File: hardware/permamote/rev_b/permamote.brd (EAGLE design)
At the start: 27 x 60 mm, 125 parts, among them J1 TC2030-JLINK-NL, J5 MICRO_USB_B_HIROSE_ZX62R-B-5P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, Q1 PMDXB950UPEL, Q10 PMDXB950UPEL, Q2 PMDXB950UPEL, Q3 PMDXB950UPEL, Q4 PMDXB950UPEL, Q5 PMDXB950UPEL, Q6 PMDXB950UPEL, Q7 PMDXB950UPEL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

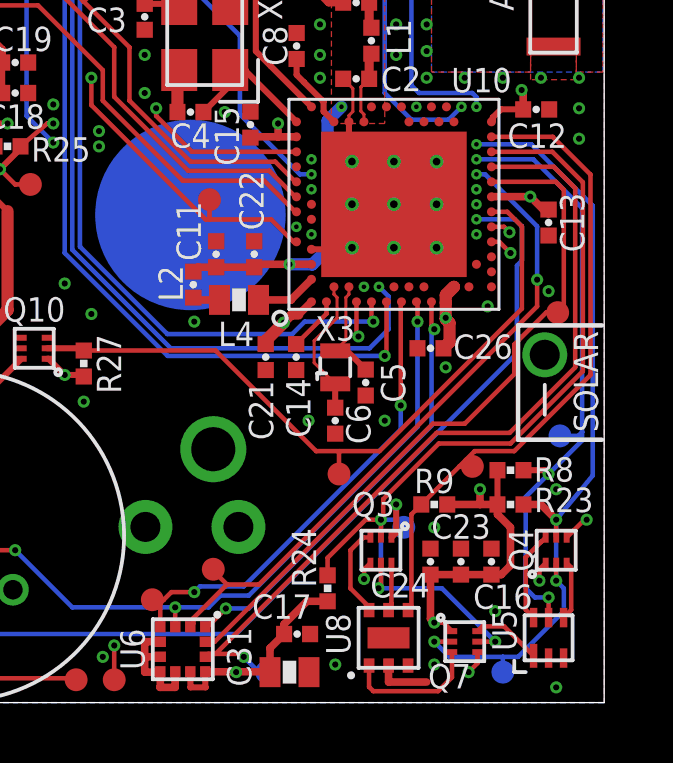
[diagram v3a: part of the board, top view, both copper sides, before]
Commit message: Switch to TCS34725 color sensor
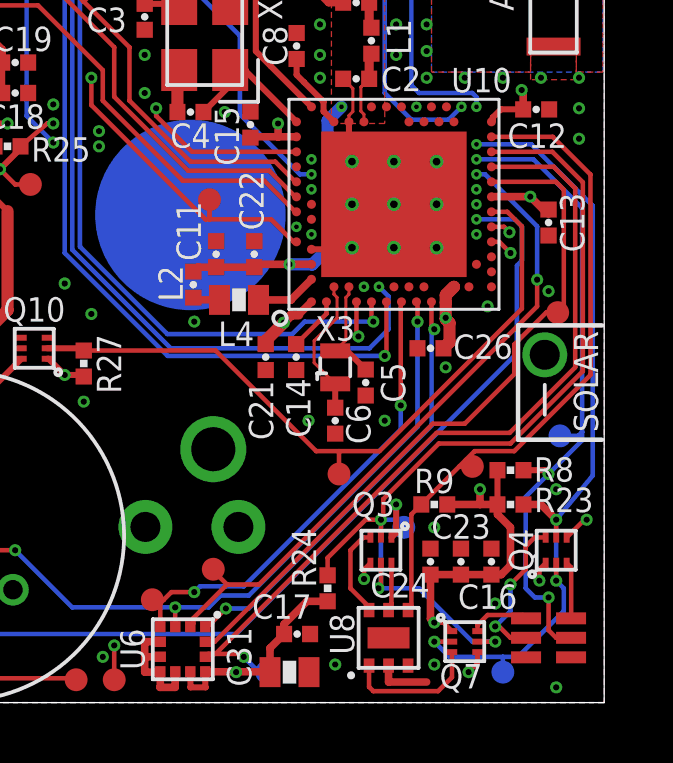
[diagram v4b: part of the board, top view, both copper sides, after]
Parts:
- removed U5: ISL29125, chips:ODFN-6-1.5MMX1.6MM
- added U12: TCS34725, chips:FN-6
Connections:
- net !CLR_INT: now also U12.5; no longer U5.5
- net GND: now also U12.3; no longer U5.3
- net N$31: now also U12.1; no longer U5.1
- net N$54: now also U12.6; no longer U5.4
- net N$55: now also U12.2; no longer U5.6
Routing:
- net N$55: track 3.06 -> 5.06 mm, vias 0 -> 2
- net !CLR_INT: track 20.9 -> 22.2 mm
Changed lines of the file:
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@@
 <?xml version="1.0" encoding="utf-8"?>
 <!DOCTYPE eagle SYSTEM "eagle.dtd">
-<eagle version="9.0.0">
+<eagle version="9.0.1">
 <drawing>
 <settings>
@@
 <attribute name="NAME" x="23.114" y="5.842" size="0.8128" layer="26" font="vector" ratio="12" rot="MR90"/>
 </element>
-<element name="U5" library="chips" package="ODFN-6-1.5MMX1.6MM" value="ISL29125" x="25.146" y="2.159" smashed="yes" rot="R90">
-<attribute name="DIGIKEY" value="ISL29125IROZ-T7ACT-ND " x="25.146" y="2.159" size="1.778" layer="27" rot="R90" display="off"/>
-<attribute name="MANUFACTURER" value="INTERSIL" x="25.146" y="2.159" size="1.778" layer="27" rot="R90" display="off"/>
-<attribute name="MPN" value="ISL29125IROZ-T7A" x="25.146" y="2.159" size="1.778" layer="27" rot="R90" display="off"/>
-<attribute name="NAME" x="23.268" y="2.409" size="0.8128" layer="25" font="vector" ratio="12" rot="R90" align="top-center"/>
-</element>
 <element name="U8" library="chips" package="UDFN-6-EXPOSED" value="MAX44009" x="19.812" y="2.159" smashed="yes" rot="R90">
 <attribute name="DIGIKEY" value="MAX44009EDT+TCT-ND" x="19.812" y="2.159" size="1.778" layer="27" rot="R90" display="off"/>
 <attribute name="MANUFACTURER" value="MAXIM" x="19.812" y="2.159" size="1.778" layer="27" rot="R90" display="off"/>
 <attribute name="MPN" value="MAX44009EDT+T" x="19.812" y="2.159" size="1.778" layer="27" rot="R90" display="off"/>
-<attribute name="NAME" x="18.542" y="2.286" size="0.8128" layer="25" font="vector" ratio="12" rot="R90" align="bottom-center"/>
+<attribute name="NAME" x="18.669" y="2.286" size="0.8128" layer="25" font="vector" ratio="12" rot="R90" align="bottom-center"/>
 </element>
 <element name="C23" library="passives" package="0402_CAP" value="1uF" x="22.225" y="4.699" smashed="yes" rot="R90">
@@
 <attribute name="DIGIKEY" value="490-6328-1-ND" x="23.241" y="4.699" size="1.778" layer="27" rot="R90" display="off"/>
 <attribute name="MPN" value="GRM155R71C104KA88J " x="23.241" y="4.699" size="1.778" layer="27" rot="R90" display="off"/>
-<attribute name="NAME" x="23.622" y="3.937" size="0.8128" layer="25" font="vector" ratio="12" rot="R180" align="bottom-center"/>
+<attribute name="NAME" x="23.114" y="3.937" size="0.8128" layer="25" font="vector" ratio="12" rot="R180" align="bottom-center"/>
 </element>
 <element name="C24" library="passives" package="0402_CAP" value="1uF" x="21.209" y="4.699" smashed="yes" rot="R90">
@@
 <attribute name="MANUFACTURER" value="NEXPERIA" x="22.352" y="2.032" size="1.778" layer="27" display="off"/>
 <attribute name="MPN" value="PMDXB950UPELZ" x="22.352" y="2.032" size="1.778" layer="27" display="off"/>
-<attribute name="NAME" x="21.844" y="1.286" size="0.8128" layer="25" font="vector" ratio="12" rot="R180" align="bottom-center"/>
+<attribute name="NAME" x="22.225" y="1.286" size="0.8128" layer="25" font="vector" ratio="12" rot="R180" align="bottom-center"/>
 <attribute name="VALUE" x="22.352" y="1.032" size="1.016" layer="27" font="vector" ratio="12" align="top-center"/>
 </element>
@@
 <element name="TP26" library="headers" package="PAD.03X.03" value="TEST-POINT" x="26.035" y="39.116" rot="MR0"/>
 <element name="TP27" library="headers" package="PAD.03X.03" value="TEST-POINT" x="26.035" y="37.084" rot="MR0"/>
+<element name="U12" library="chips" package="FN-6" value="TCS34725" x="25.146" y="2.159" smashed="yes">
+<attribute name="DIGIKEY" value="TCS34725FNCT-ND" x="25.146" y="2.159" size="1.778" layer="27" display="off"/>
+<attribute name="NAME" x="26.654" y="4.315" size="0.8128" layer="23" font="vector" ratio="12" rot="R180"/>
+</element>
 </elements>
 <signals>
@@
 <contactref element="U7" pad="3"/>
 <contactref element="C30" pad="2"/>
-<contactref element="U5" pad="3"/>
 <contactref element="U8" pad="2"/>
 <contactref element="U8" pad="EP"/>
@@
 <via x="18.034" y="1.27" extent="1-16" drill="0.2032"/>
 <via x="25.4" y="7.112" extent="1-16" drill="0.2032"/>
-<via x="23.368" y="3.048" extent="1-16" drill="0.2032"/>
+<via x="23.368" y="3.302" extent="1-16" drill="0.2032"/>
 <via x="25.4" y="0.508" extent="1-16" drill="0.2032"/>
 <via x="20.066" y="23.622" extent="1-16" drill="0.2032"/>
@@
 <wire x1="19.812" y1="1.234" x2="19.812" y2="0.6858" width="0.254" layer="1"/>
 <wire x1="19.812" y1="0.6858" x2="21.082" y2="0.6858" width="0.254" layer="1"/>
+<contactref element="U12" pad="3"/>
 </signal>
 <signal name="N$8">
@@
 </signal>
 <signal name="!CLR_INT">
-<contactref element="U5" pad="5"/>
 <contactref element="R8" pad="1"/>
 <contactref element="U10" pad="AC19"/>
 <via x="22.742" y="18.11" extent="1-16" drill="0.1524"/>
 <via x="25.146" y="3.5052" extent="1-16" drill="0.2032"/>
-<wire x1="25.146" y1="2.834" x2="25.146" y2="3.5052" width="0.1524" layer="1"/>
 <wire x1="25.146" y1="3.5052" x2="24.6888" y2="3.5052" width="0.1524" layer="16"/>
 <wire x1="24.6888" y1="3.5052" x2="24.384" y2="3.81" width="0.1524" layer="16"/>
@@
 <wire x1="25.527" y1="8.89" x2="26.136971875" y2="8.89" width="0.1524" layer="16"/>
 <wire x1="26.136971875" y1="8.89" x2="26.263971875" y2="9.017" width="0.1524" layer="16"/>
+<contactref element="U12" pad="5"/>
+<wire x1="25.896" y1="2.159" x2="25.4" y2="2.159" width="0.1524" layer="1"/>
+<wire x1="25.4" y1="2.159" x2="25.146" y2="2.413" width="0.1524" layer="1"/>
+<wire x1="25.146" y1="2.413" x2="25.146" y2="3.5052" width="0.1524" layer="1"/>
 </signal>
 <signal name="!LT_INT">
@@
 <via x="23.368" y="2.032" extent="1-16" drill="0.2032"/>
 <wire x1="19.4762" y1="3.81" x2="19.558" y2="3.81" width="0.1524" layer="16"/>
-<wire x1="19.558" y1="3.81" x2="21.59" y2="3.81" width="0.1524" layer="16"/>
-<wire x1="21.59" y1="3.81" x2="23.368" y2="2.032" width="0.1524" layer="16"/>
 <wire x1="19.558" y1="5.505" x2="19.558" y2="6.096" width="0.1524" layer="1"/>
 <via x="19.558" y="6.096" extent="1-16" drill="0.2032"/>
@@
 <wire x1="26.289" y1="11.049" x2="23.876" y2="8.636" width="0.1524" layer="1"/>
 <wire x1="23.876" y1="8.636" x2="21.4873375" y2="8.636" width="0.1524" layer="1"/>
-<wire x1="26.289" y1="17.344" x2="26.289" y2="16.383" width="0.1524" layer="1"/>
-<wire x1="26.289" y1="16.383" x2="26.289" y2="11.049" width="0.1524" layer="1"/>
+<wire x1="26.289" y1="17.344" x2="26.289" y2="11.049" width="0.1524" layer="1"/>
+<wire x1="23.368" y1="2.032" x2="22.606" y2="2.032" width="0.1524" layer="16"/>
+<wire x1="20.828" y1="3.81" x2="19.558" y2="3.81" width="0.1524" layer="16"/>
+<wire x1="22.606" y1="2.032" x2="20.828" y2="3.81" width="0.1524" layer="16"/>
 </signal>
 <signal name="VREF_SAMP">
@@
 </signal>
 <signal name="N$31">
-<contactref element="U5" pad="1"/>
 <contactref element="Q7" pad="6"/>
-<wire x1="22.777" y1="2.382" x2="22.935" y2="2.54" width="0.1524" layer="1"/>
-<wire x1="23.665" y1="2.54" x2="24.646" y2="1.559" width="0.1524" layer="1"/>
-<wire x1="22.935" y1="2.54" x2="23.665" y2="2.54" width="0.1524" layer="1"/>
+<contactref element="U12" pad="1"/>
+<wire x1="22.777" y1="2.382" x2="22.777" y2="2.584" width="0.1524" layer="1"/>
+<wire x1="22.777" y1="2.584" x2="23.114" y2="2.921" width="0.1524" layer="1"/>
+<wire x1="23.114" y1="2.921" x2="24.284" y2="2.921" width="0.1524" layer="1"/>
+<wire x1="24.284" y1="2.921" x2="24.396" y2="2.809" width="0.1524" layer="1"/>
 </signal>
 <signal name="N$20">
@@
 <signal name="N$54">
 <contactref element="Q4" pad="3"/>
-<contactref element="U5" pad="4"/>
-<wire x1="25.9" y1="4.505" x2="25.75" y2="4.655" width="0.1524" layer="1"/>
-<wire x1="25.646" y1="2.834" x2="25.9" y2="3.088" width="0.1524" layer="1"/>
-<wire x1="25.9" y1="3.088" x2="25.9" y2="4.505" width="0.1524" layer="1"/>
+<wire x1="25.75" y1="4.655" x2="25.9" y2="4.505" width="0.1524" layer="1"/>
+<contactref element="U12" pad="6"/>
+<wire x1="25.9" y1="2.813" x2="25.896" y2="2.809" width="0.1524" layer="1"/>
+<wire x1="25.9" y1="4.505" x2="25.9" y2="2.813" width="0.1524" layer="1"/>
 </signal>
 <signal name="N$55">
 <contactref element="Q4" pad="6"/>
-<contactref element="U5" pad="6"/>
-<wire x1="25.05" y1="5.505" x2="24.902" y2="5.357" width="0.1524" layer="1"/>
-<wire x1="24.902" y1="5.357" x2="24.89739375" y2="5.357" width="0.1524" layer="1"/>
-<wire x1="24.384" y1="4.84360625" x2="24.89739375" y2="5.357" width="0.1524" layer="1"/>
-<wire x1="24.646" y1="2.834" x2="24.384" y2="3.096" width="0.1524" layer="1"/>
-<wire x1="24.384" y1="3.096" x2="24.384" y2="4.84360625" width="0.1524" layer="1"/>
+<contactref element="U12" pad="2"/>
+<via x="23.368" y="2.54" extent="1-16" drill="0.2032"/>
+<wire x1="23.368" y1="2.54" x2="23.495" y2="2.54" width="0.1524" layer="1"/>
+<wire x1="23.495" y1="2.54" x2="23.876" y2="2.159" width="0.1524" layer="1"/>
+<wire x1="23.876" y1="2.159" x2="24.396" y2="2.159" width="0.1524" layer="1"/>
+<via x="23.876" y="3.937" extent="1-16" drill="0.2032"/>
+<wire x1="23.876" y1="3.937" x2="23.876" y2="3.048" width="0.1524" layer="16"/>
+<wire x1="23.876" y1="3.048" x2="23.368" y2="2.54" width="0.1524" layer="16"/>
+<wire x1="25.05" y1="5.505" x2="24.682" y2="5.505" width="0.1524" layer="1"/>
+<wire x1="24.682" y1="5.505" x2="24.384" y2="5.207" width="0.1524" layer="1"/>
+<wire x1="24.384" y1="5.207" x2="24.384" y2="4.445" width="0.1524" layer="1"/>
+<wire x1="24.384" y1="4.445" x2="23.876" y2="3.937" width="0.1524" layer="1"/>
 </signal>
 <signal name="LBST">

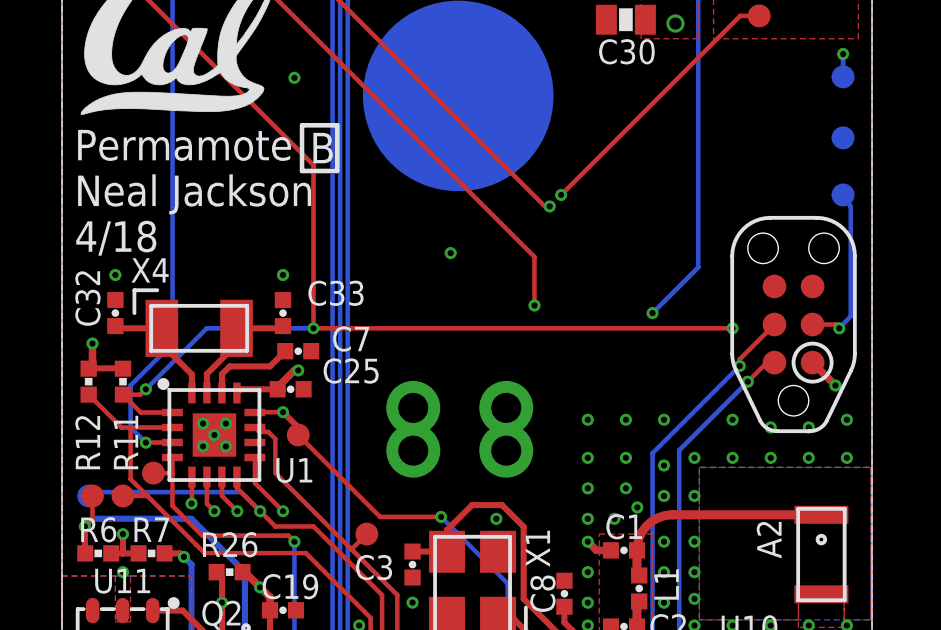
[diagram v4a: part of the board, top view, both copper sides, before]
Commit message: move programmer
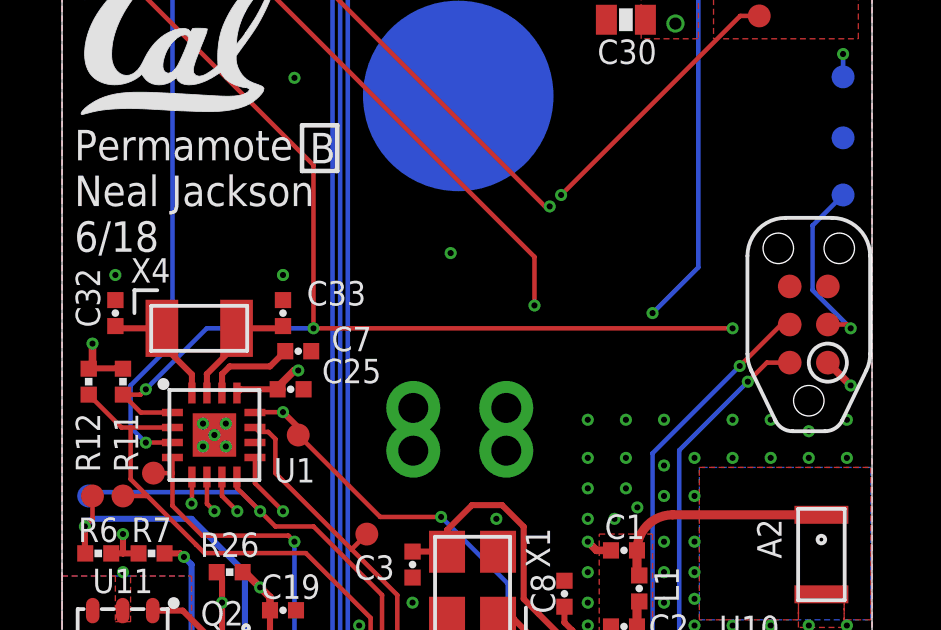
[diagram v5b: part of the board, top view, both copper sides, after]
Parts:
- moved J1 0.51 mm to (24.9, 30.9)
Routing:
- net !RST: track 65.3 -> 66.3 mm
- net SWDIO: track 13.1 -> 13.6 mm
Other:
- board text added: "Permamote Neal Jackson 6/18"
- board text removed: "Permamote Neal Jackson 4/18"
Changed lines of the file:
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@@
 <text x="0.413" y="37.349" size="1.016" layer="25" font="vector" ratio="12" align="top-left">Permamote
 Neal Jackson
-4/18</text>
+6/18</text>
 <polygon width="0.1016" layer="41">
 <vertex x="12.446" y="1.7907"/>
@@
 <attribute name="NAME" x="7.62" y="21.717" size="0.8128" layer="25" font="vector" ratio="12" align="bottom-center"/>
 </element>
-<element name="J1" library="connector" package="TC2030-IDC-NL" value="TC2030-JLINK-NL" x="24.384" y="30.861" smashed="yes" rot="R90">
-<attribute name="VALUE" x="30.4165" y="30.861" size="1.016" layer="27" font="vector" ratio="12" rot="R90" align="bottom-center"/>
+<element name="J1" library="connector" package="TC2030-IDC-NL" value="TC2030-JLINK-NL" x="24.892" y="30.861" smashed="yes" rot="R90">
+<attribute name="VALUE" x="30.9245" y="30.861" size="1.016" layer="27" font="vector" ratio="12" rot="R90" align="bottom-center"/>
 </element>
 <element name="R23" library="passives" package="0402_RES" value="100M" x="23.876" y="6.604" smashed="yes" rot="R180">
@@
 <via x="20.066" y="27.686" extent="1-16" drill="0.2032"/>
 <via x="22.352" y="27.686" extent="1-16" drill="0.2032"/>
-<via x="23.622" y="27.432" extent="1-16" drill="0.2032"/>
-<via x="24.892" y="27.432" extent="1-16" drill="0.2032"/>
+<via x="23.622" y="27.686" extent="1-16" drill="0.2032"/>
+<via x="24.892" y="27.305" extent="1-16" drill="0.2032"/>
 <via x="26.162" y="27.686" extent="1-16" drill="0.2032"/>
 <contactref element="U2" pad="5"/>
@@
 <wire x1="6.93293125" y1="21.336" x2="6.93293125" y2="21.76906875" width="0.254" layer="1"/>
 <wire x1="6.93293125" y1="21.76906875" x2="6.604" y2="22.098" width="0.254" layer="1"/>
-<via x="25.781" y="28.829" extent="1-16" drill="0.2032"/>
+<via x="26.289" y="28.829" extent="1-16" drill="0.2032"/>
 <wire x1="16.129" y1="19.304" x2="16.129" y2="18.86" width="0.254" layer="1"/>
 <wire x1="16.33093125" y1="2.286" x2="16.33093125" y2="2.61493125" width="0.254" layer="1"/>
@@
 <wire x1="9.017" y1="10.922" x2="9.59993125" y2="10.922" width="0.2032" layer="1"/>
 <wire x1="9.59993125" y1="10.922" x2="9.652" y2="10.86993125" width="0.2032" layer="1"/>
-<wire x1="25.019" y1="29.591" x2="25.781" y2="28.829" width="0.254" layer="1"/>
+<wire x1="25.527" y1="29.591" x2="26.289" y2="28.829" width="0.254" layer="1"/>
 <wire x1="21.992" y1="13.86" x2="21.717" y2="13.585" width="0.4064" layer="1"/>
 <wire x1="21.717" y1="13.585" x2="21.717" y2="13.335" width="0.4064" layer="1"/>
@@
 <via x="22.742" y="16.61" extent="1-16" drill="0.1524"/>
 <contactref element="SJ3" pad="1"/>
-<wire x1="22.352" y1="30.734" x2="25.908" y2="30.734" width="0.1524" layer="15"/>
-<via x="25.908" y="30.734" extent="1-16" drill="0.2032"/>
-<wire x1="25.908" y1="30.734" x2="25.781" y2="30.861" width="0.1524" layer="1"/>
-<wire x1="25.781" y1="30.861" x2="25.019" y2="30.861" width="0.1524" layer="1"/>
+<wire x1="22.352" y1="30.734" x2="26.289" y2="30.734" width="0.1524" layer="15"/>
+<via x="26.289" y="30.734" extent="1-16" drill="0.2032"/>
+<wire x1="26.289" y1="30.734" x2="26.162" y2="30.861" width="0.1524" layer="1"/>
+<wire x1="26.162" y1="30.861" x2="25.527" y2="30.861" width="0.1524" layer="1"/>
 <wire x1="2.032" y1="28.52293125" x2="2.62693125" y2="27.928" width="0.1524" layer="1"/>
 <wire x1="2.62693125" y1="27.928" x2="3.68" y2="27.928" width="0.1524" layer="1"/>
@@
 <wire x1="20.574" y1="28.956" x2="22.352" y2="30.734" width="0.1524" layer="15"/>
 <wire x1="20.574" y1="20.574" x2="20.574" y2="28.956" width="0.1524" layer="15"/>
-<wire x1="25.908" y1="30.734" x2="25.908" y2="30.7467625" width="0.1524" layer="16"/>
-<wire x1="25.908" y1="30.7467625" x2="26.289" y2="31.1277625" width="0.1524" layer="16"/>
-<wire x1="26.289" y1="31.1277625" x2="26.289" y2="34.798" width="0.1524" layer="16"/>
 <wire x1="2.794" y1="28.702" x2="4.826" y2="30.734" width="0.1524" layer="16"/>
-<wire x1="26.289" y1="34.798" x2="26.035" y2="35.179" width="0.1524" layer="16"/>
 <wire x1="4.826" y1="30.734" x2="8.382" y2="30.734" width="0.1524" layer="16"/>
 <via x="8.382" y="30.734" extent="1-16" drill="0.2032"/>
@@
 <wire x1="1.27" y1="43.2871" x2="8.382" y2="36.1751" width="0.1524" layer="1"/>
 <wire x1="8.382" y1="36.1751" x2="8.382" y2="30.734" width="0.1524" layer="1"/>
+<wire x1="26.035" y1="35.179" x2="25.019" y2="34.163" width="0.1524" layer="16"/>
+<wire x1="25.019" y1="34.163" x2="25.019" y2="32.004" width="0.1524" layer="16"/>
+<wire x1="25.019" y1="32.004" x2="26.289" y2="30.734" width="0.1524" layer="16"/>
 </signal>
 <signal name="!RTC_IRQ1">
@@
 <wire x1="20.828" y1="20.32" x2="22.606" y2="20.32" width="0.1524" layer="16"/>
 <wire x1="22.86" y1="28.956" x2="20.574" y2="26.67" width="0.1524" layer="16"/>
-<wire x1="22.86" y1="28.956" x2="23.495" y2="29.591" width="0.1524" layer="1"/>
-<wire x1="23.495" y1="29.591" x2="23.749" y2="29.591" width="0.1524" layer="1"/>
 <via x="22.86" y="28.956" extent="1-16" drill="0.2032"/>
 <wire x1="20.574" y1="26.67" x2="20.574" y2="20.574" width="0.1524" layer="16"/>
 <wire x1="20.574" y1="20.574" x2="20.828" y2="20.32" width="0.1524" layer="16"/>
+<wire x1="22.86" y1="28.956" x2="23.495" y2="29.591" width="0.1524" layer="1"/>
+<wire x1="23.495" y1="29.591" x2="24.257" y2="29.591" width="0.1524" layer="1"/>
 </signal>
 <signal name="RTC_CS">
@@
 <contactref element="U10" pad="AA24"/>
 <via x="22.591865625" y="29.478134375" extent="1-16" drill="0.2032"/>
-<wire x1="23.749" y1="30.861" x2="22.591865625" y2="29.703865625" width="0.1524" layer="1"/>
-<wire x1="22.591865625" y1="29.703865625" x2="22.591865625" y2="29.478134375" width="0.1524" layer="1"/>
 <via x="22.242" y="19.86" extent="1-16" drill="0.1524"/>
 <wire x1="22.242" y1="19.86" x2="21.813" y2="19.431" width="0.1524" layer="16"/>
@@
 <wire x1="19.685" y1="20.32" x2="19.685" y2="26.57126875" width="0.1524" layer="16"/>
 <wire x1="19.685" y1="26.57126875" x2="22.591865625" y2="29.478134375" width="0.1524" layer="16"/>
+<wire x1="22.591865625" y1="29.478134375" x2="23.97473125" y2="30.861" width="0.1524" layer="1"/>
+<wire x1="23.97473125" y1="30.861" x2="24.257" y2="30.861" width="0.1524" layer="1"/>
 </signal>
 <signal name="N$41">
